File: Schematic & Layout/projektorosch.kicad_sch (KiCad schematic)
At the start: 39 parts, among them J1 Power barrel plug, J2 RJ12, U1 ATmega328-P, U2 MAX232, Y1 Crystal

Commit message: design pcb - first try
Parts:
- removed C1: 100nF, Capacitor_SMD:C_0805_2012Metric_Pad1.18x1.45mm_HandSolder, symbol Device:C
- removed R12: R, Resistor_SMD:R_0805_2012Metric_Pad1.20x1.40mm_HandSolder, symbol Device:R
- removed RESET1: SW_SPST, Button_Switch_SMD:SW_Push_1P1T_NO_6x6mm_H9.5mm, symbol Switch:SW_SPST
- D2: footprint Diode_SMD:D_0805_2012Metric_Pad1.15x1.40mm_HandSolder -> Diode_THT:D_DO-15_P2.54mm_Vertical_KathodeUp
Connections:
- net BTN1: now also U1.12 (PD6); no longer U1.23 (PC0)
- net BTN3: now also U1.6 (PD4); no longer U1.25 (PC2)
- net CTS: now also J2.5; no longer J2.6
- net GND: now also J2.1; no longer J2.3
- net RTS: now also J2.6; no longer J2.5
- net RX: now also J2.3; no longer J2.1
- net TX: no longer U1.2 (PD0), U2.12 (R1OUT)
- net at U1.28 (PC5): now also D2.2 (A)
- new net: U1.2 (PD0), U2.12 (R1OUT)
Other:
- moved on the sheet: C9

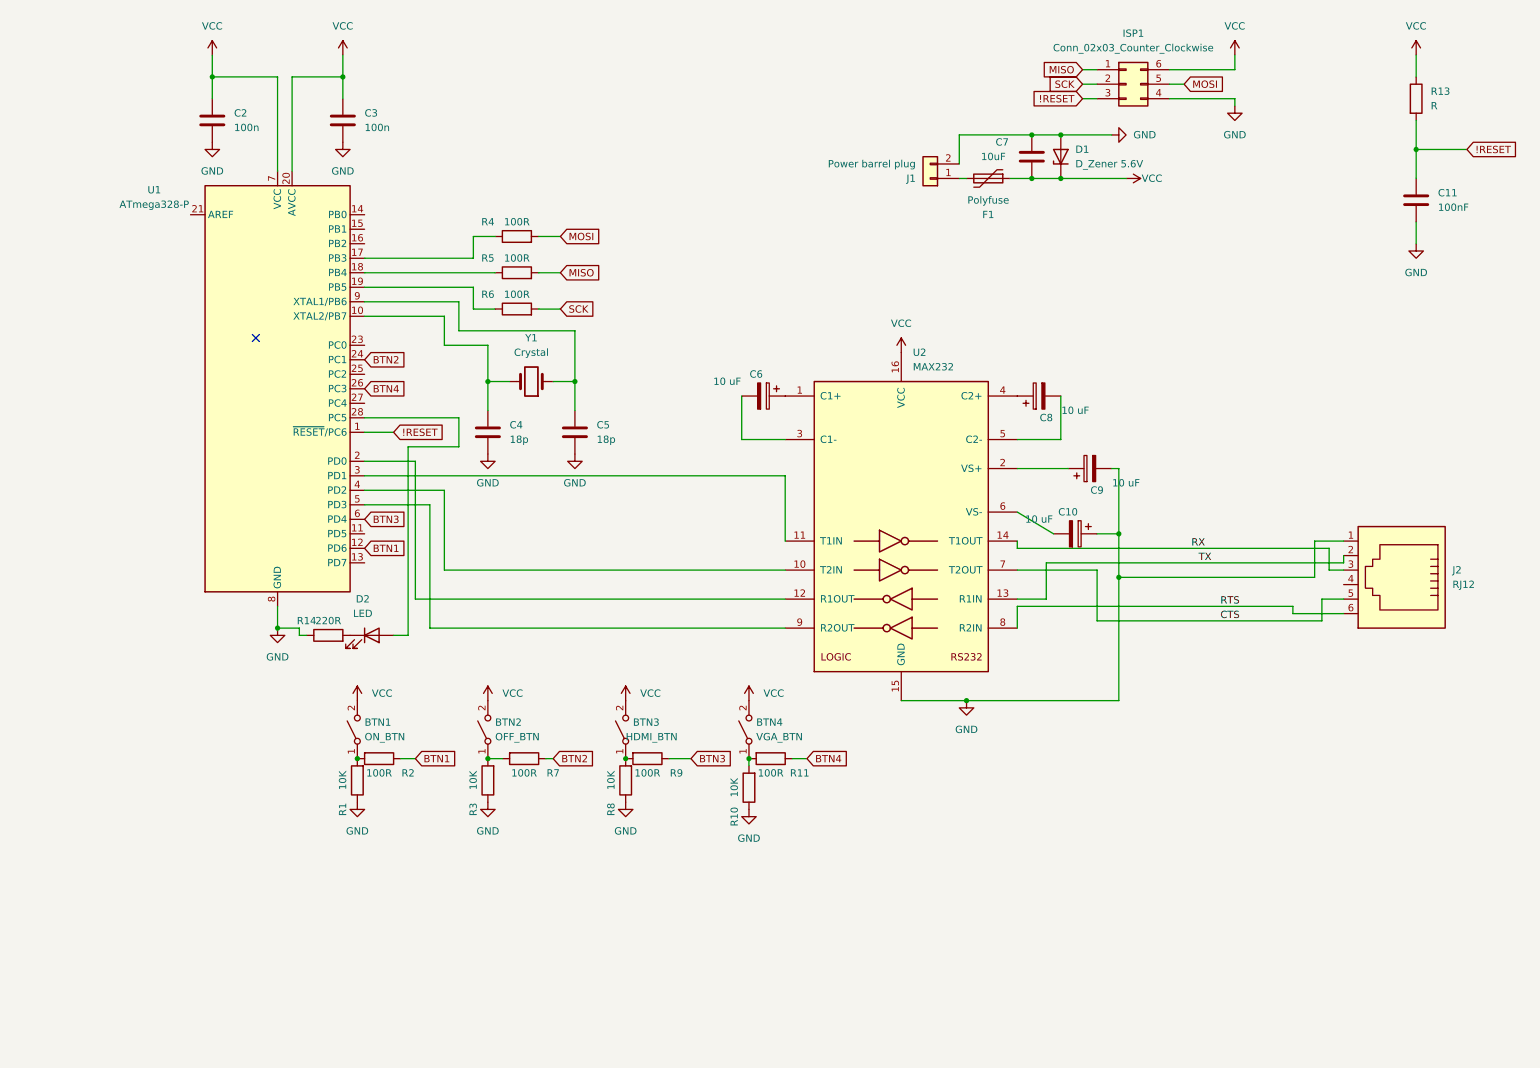
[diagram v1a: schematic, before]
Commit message: redesign layout for attiny3216
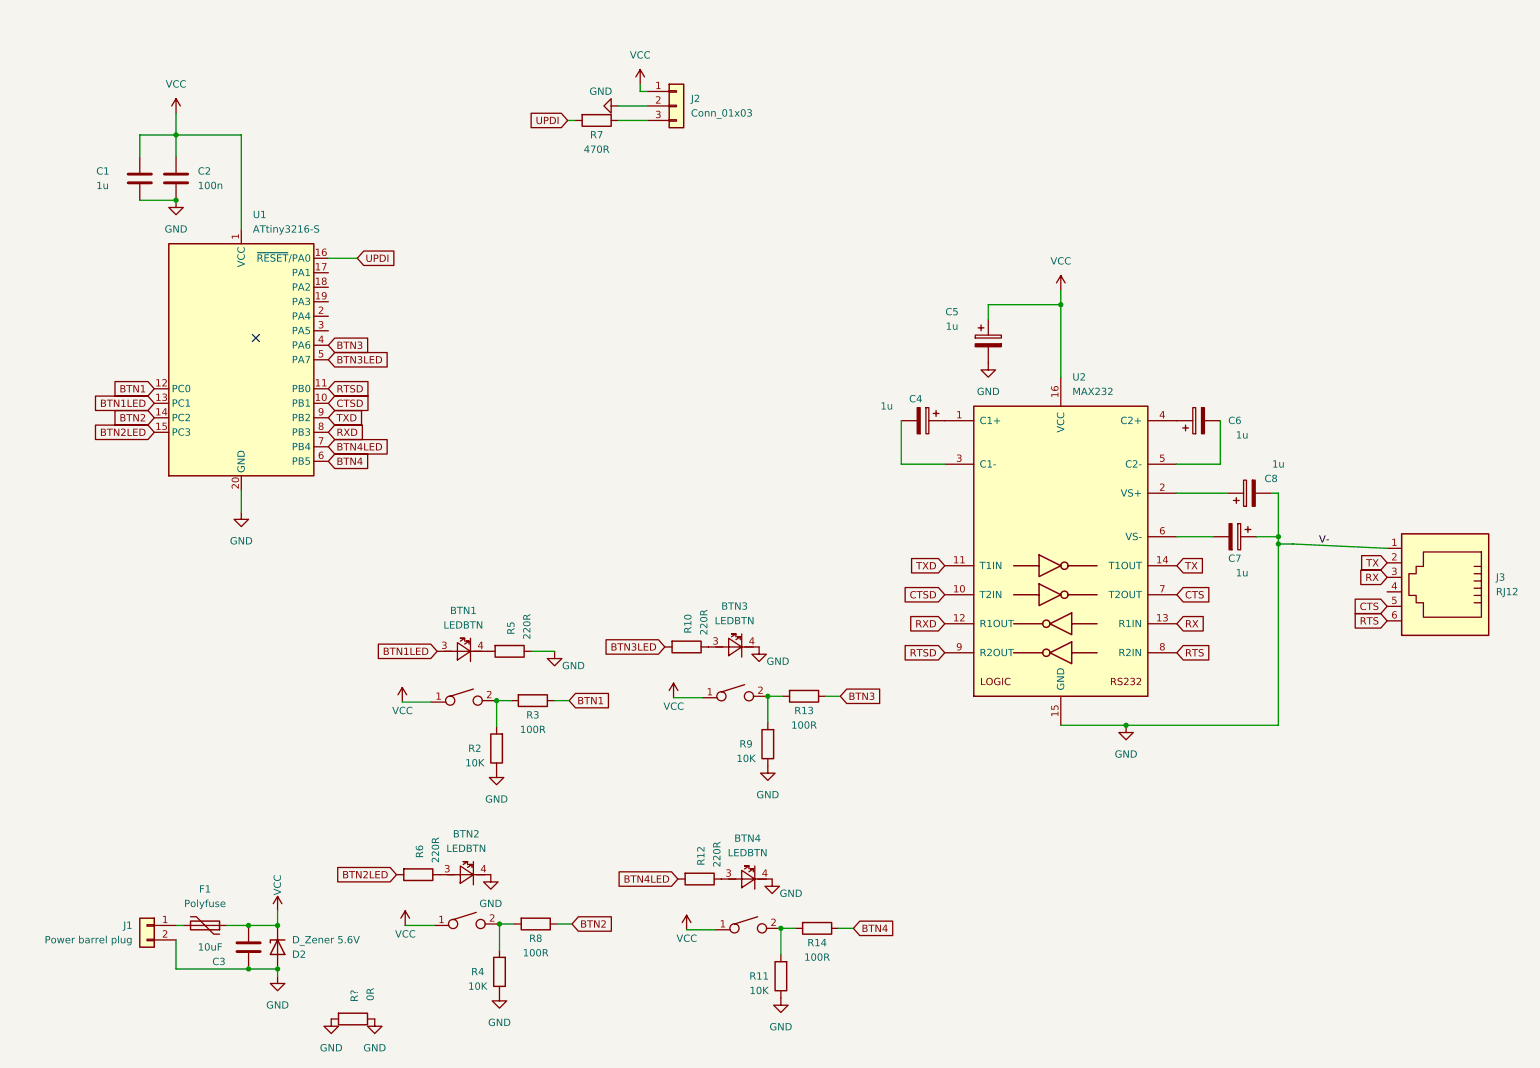
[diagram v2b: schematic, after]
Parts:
- removed BTN1: ON_BTN, Button_Switch_SMD:SW_Push_1P1T_NO_6x6mm_H9.5mm, symbol Switch:SW_SPST
- removed BTN2: OFF_BTN, Button_Switch_SMD:SW_Push_1P1T_NO_6x6mm_H9.5mm, symbol Switch:SW_SPST
- removed BTN3: HDMI_BTN, Button_Switch_SMD:SW_Push_1P1T_NO_6x6mm_H9.5mm, symbol Switch:SW_SPST
- removed BTN4: VGA_BTN, Button_Switch_SMD:SW_Push_1P1T_NO_6x6mm_H9.5mm, symbol Switch:SW_SPST
- removed C11: 100nF, Capacitor_SMD:C_0805_2012Metric_Pad1.18x1.45mm_HandSolder, symbol Device:C
- removed C3: 100n, Capacitor_SMD:C_0805_2012Metric_Pad1.18x1.45mm_HandSolder, symbol Device:C
- removed C4, C5: 18p, Capacitor_SMD:C_0603_1608Metric_Pad1.08x0.95mm_HandSolder, symbol Device:C
- removed D2: LED, Diode_THT:D_DO-15_P2.54mm_Vertical_KathodeUp, symbol Device:LED
- removed ISP1: Conn_02x03_Counter_Clockwise, Connector_PinHeader_2.00mm:PinHeader_2x03_P2.00mm_Vertical_SMD, symbol Connector_Generic:Conn_02x03_Counter_Clockwise
- removed J2: RJ12, Connector_RJ:RJ12_Amphenol_54601, symbol Connector:RJ12
- removed R3: 10K, Resistor_SMD:R_0805_2012Metric_Pad1.20x1.40mm_HandSolder, symbol Device:R
- removed U1: ATmega328-P, Package_DFN_QFN:QFN-32-1EP_5x5mm_P0.5mm_EP3.6x3.6mm_ThermalVias, symbol MCU_Microchip_ATmega:ATmega328-P
- removed Y1: Crystal, Crystal:Crystal_SMD_3225-4Pin_3.2x2.5mm_HandSoldering, symbol Device:Crystal
- added BTN1, BTN2, BTN3, BTN4: LEDBTN, ledbtn_footprint:LBTN, symbol projektorosch:LEDBTN
- added C1: 1u, Capacitor_Tantalum_SMD:CP_EIA-3216-10_Kemet-I_Pad1.58x1.35mm_HandSolder, symbol Device:C
- added C5: 1u, Capacitor_Tantalum_SMD:CP_EIA-3216-10_Kemet-I_Pad1.58x1.35mm_HandSolder, symbol Device:C_Polarized
- added J2: Conn_01x03, Connector_PinHeader_2.54mm:PinHeader_1x03_P2.54mm_Vertical, symbol Connector_Generic:Conn_01x03
- added J3: RJ12, Connector_RJ:RJ12_Amphenol_54601, symbol Connector:RJ12
- added R12: 220R, Resistor_SMD:R_0805_2012Metric_Pad1.20x1.40mm_HandSolder, symbol Device:R
- added R?: 0R, Resistor_SMD:R_0805_2012Metric_Pad1.20x1.40mm_HandSolder, symbol Device:R
- added U1: ATtiny3216-S, Package_SO:SOIC-20W_7.5x12.8mm_P1.27mm, symbol MCU_Microchip_ATtiny:ATtiny3216-S
- C3: renamed from C7; footprint Capacitor_SMD:CP_Elec_5x5.7 -> Capacitor_Tantalum_SMD:CP_EIA-3216-12_Kemet-S_Pad1.58x1.35mm_HandSolder
- C4: renamed from C6; value 10 uF -> 1u; footprint Capacitor_SMD:CP_Elec_5x5.7 -> Capacitor_Tantalum_SMD:CP_EIA-3216-10_Kemet-I_Pad1.58x1.35mm_HandSolder
- C6: renamed from C8; value 10 uF -> 1u; footprint Capacitor_SMD:CP_Elec_5x5.7 -> Capacitor_Tantalum_SMD:CP_EIA-3216-10_Kemet-I_Pad1.58x1.35mm_HandSolder
- C7: renamed from C10; value 10 uF -> 1u; footprint Capacitor_SMD:CP_Elec_5x5.7 -> Capacitor_Tantalum_SMD:CP_EIA-3216-10_Kemet-I_Pad1.58x1.35mm_HandSolder
- C8: renamed from C9; value 10 uF -> 1u; footprint Capacitor_SMD:CP_Elec_5x5.7 -> Capacitor_Tantalum_SMD:CP_EIA-3216-10_Kemet-I_Pad1.58x1.35mm_HandSolder
- F1: footprint Fuse:Fuse_BelFuse_0ZRE0005FF_L8.3mm_W3.8mm -> Fuse:Fuse_1812_4532Metric_Pad1.30x3.40mm_HandSolder
- R10: value 10K -> 220R
- R11, R4, R9: value 100R -> 10K
- R13: value R -> 100R
- R14: value 220R -> 100R
- R5, R6: value 100R -> 220R
- R7: value 100R -> 470R
- R8: value 10K -> 100R
- U2: footprint Package_SO:HTSSOP-16-1EP_4.4x5mm_P0.65mm_EP3.4x5mm_Mask2.46x2.31mm -> Package_DIP:DIP-16_W7.62mm
- renumbered D1 to D2, R1 to R2, R2 to R3
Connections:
- net !RESET is gone; now on an unnamed net: R13.2
- net BTN1: now also U1.12 (PC0)
- net BTN2: now also R8.1, U1.14 (PC2); no longer R7.1
- net BTN3: now also R13.1, U1.4 (PA6); no longer R9.1
- net BTN4: now also R14.1, U1.6 (PB5); no longer R11.1
- net CTS: now also J3.5
- net GND: now also R11.1, R4.1, R5.1, R9.1, BTN2.4, BTN3.4, BTN4.4, C1.2, C5.2, J2.2 (Pin_2), J3.1, R?.1, R?.2, U1.20 (GND); no longer R10.1, R14.1, R8.1
- net RTS: now also J3.6
- net RX: now also U2.13 (R1IN), J3.3; no longer U2.14 (T1OUT)
- net TX: now also U2.14 (T1OUT), J3.2; no longer U2.13 (R1IN)
- net VCC: now also BTN1.1, BTN2.1, BTN3.1, BTN4.1, C1.1, C5.1, J2.1 (Pin_1), U1.1 (VCC); no longer R13.1
- net at R6.1: now also BTN2.3
- net UPDI: now reaches R7.2
- net UPDI: now also U1.16 (~{RESET}/PA0)
- net at R11.2: now also R14.2, BTN4.2; no longer R10.2
- net at R2.2, R3.2: now also BTN1.2
- net CTSD: now reaches U2.10 (T2IN)
- net CTSD: now also U1.10 (PB1)
- net TXD: now reaches U2.11 (T1IN)
- net TXD: now also U1.9 (PB2)
- net RXD: now reaches U2.12 (R1OUT)
- net RXD: now also U1.8 (PB3)
- net RTSD: now reaches U2.9 (R2OUT)
- net RTSD: now also U1.11 (PB0)
- net at R9.2: now also BTN3.2; no longer R8.2
- net MISO: no longer names the net of R5.2
- net MISO: now also BTN1.4
- net MOSI: no longer names the net of R4.2
- net MOSI: now also R8.2, BTN2.2
- net SCK renamed BTN2LED
- net BTN2LED: now also U1.15 (PC3)
- new net: BTN4.3, R12.1
- new net: J2.3 (Pin_3), R7.1
- new net: BTN3.3, R10.1
- new net BTN1LED: BTN1.3, U1.13 (PC1)
- new net BTN3LED: R10.2, U1.5 (PA7)
- new net BTN4LED: R12.2, U1.7 (PB4)
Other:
- moved on the sheet: C2, C3, C4, C6, C7, C8, D2, F1, J1, R2, R3, U2

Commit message: attinty3216-remeljuk-final
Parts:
- removed J1: Power barrel plug, Connector_BarrelJack:BarrelJack_CLIFF_FC681465S_SMT_Horizontal, symbol Connector_Generic:Conn_01x02
- removed R11, R2, R4, R9: 10K, Resistor_SMD:R_0805_2012Metric_Pad1.20x1.40mm_HandSolder, symbol Device:R
- removed R13, R14, R3, R8: 100R, Resistor_SMD:R_0805_2012Metric_Pad1.20x1.40mm_HandSolder, symbol Device:R
- removed R?: 0R, Resistor_SMD:R_0805_2012Metric_Pad1.20x1.40mm_HandSolder, symbol Device:R
- added J1: Barrel_Jack_Switch, Connector_BarrelJack:BarrelJack_Horizontal, symbol Connector:Barrel_Jack_Switch
- renumbered D2 to D1, R12 to R10, R6 to R2, R7 to R8, R10 to R9
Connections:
- net BTN1: now also BTN1.2, U1.14 (PC2); no longer U1.12 (PC0)
- net BTN1LED: now also R5.2, U1.15 (PC3); no longer BTN1.3, U1.13 (PC1)
- net BTN2: now also BTN2.2, U1.12 (PC0); no longer U1.14 (PC2)
- net BTN2LED: now also U1.13 (PC1); no longer U1.15 (PC3)
- net BTN3: now also BTN3.2, U1.17 (PA1); no longer U1.4 (PA6)
- net BTN3LED: now also U1.18 (PA2); no longer U1.5 (PA7)
- net BTN4: now also BTN4.2, U1.2 (PA4); no longer U1.6 (PB5)
- net BTN4LED: now also U1.5 (PA7); no longer U1.7 (PB4)
- net GND: now also BTN1.1, BTN1.4, BTN2.1, BTN3.1, BTN4.1, U1.3 (PA5), U1.4 (PA6), J1.2, J1.3; no longer R5.1
- net VCC: no longer BTN1.1, BTN2.1, BTN3.1, BTN4.1
- net at F1.2: now also J1.1
- new net: BTN1.3, R5.1
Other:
- moved on the sheet: R5

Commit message: SEM ProjektoroSCH Revision 2
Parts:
- removed BTN1, BTN2, BTN3, BTN4: LEDBTN, ledbtn_footprint:LBTN, symbol projektorosch:LEDBTN
- removed C1: 1u, Capacitor_Tantalum_SMD:CP_EIA-3216-10_Kemet-I_Pad1.58x1.35mm_HandSolder, symbol Device:C
- removed C2: 100n, Capacitor_SMD:C_0805_2012Metric_Pad1.18x1.45mm_HandSolder, symbol Device:C
- removed C3: 10uF, Capacitor_Tantalum_SMD:CP_EIA-3216-12_Kemet-S_Pad1.58x1.35mm_HandSolder, symbol Device:C
- removed C5, C7, C8: 1u, Capacitor_Tantalum_SMD:CP_EIA-3216-10_Kemet-I_Pad1.58x1.35mm_HandSolder, symbol Device:C_Polarized
- removed D1: D_Zener 5.6V, Diode_SMD:Nexperia_CFP3_SOD-123W, symbol Device:D_Zener
- removed F1: Polyfuse, Fuse:Fuse_1812_4532Metric_Pad1.30x3.40mm_HandSolder, symbol Device:Polyfuse
- removed J1: Barrel_Jack_Switch, Connector_BarrelJack:BarrelJack_Horizontal, symbol Connector:Barrel_Jack_Switch
- removed J2: Conn_01x03, Connector_PinHeader_2.54mm:PinHeader_1x03_P2.54mm_Vertical, symbol Connector_Generic:Conn_01x03
- removed J3: RJ12, Connector_RJ:RJ12_Amphenol_54601, symbol Connector:RJ12
- removed R10, R2, R5, R9: 220R, Resistor_SMD:R_0805_2012Metric_Pad1.20x1.40mm_HandSolder, symbol Device:R
- removed R8: 470R, Resistor_SMD:R_0805_2012Metric_Pad1.20x1.40mm_HandSolder, symbol Device:R
- removed U1: ATtiny3216-S, Package_SO:SOIC-20W_7.5x12.8mm_P1.27mm, symbol MCU_Microchip_ATtiny:ATtiny3216-S
- removed U2: MAX232, Package_DIP:DIP-16_W7.62mm, symbol Interface_UART:MAX232
- added C1, C2, C3: 0.1uF, Capacitor_SMD:C_0805_2012Metric_Pad1.18x1.45mm_HandSolder, symbol Device:C_Polarized
- added C10, C9: 22pF, Capacitor_SMD:C_0805_2012Metric_Pad1.18x1.45mm_HandSolder, symbol Device:C_Small
- added C5, C7, C8: 0.1uF, Capacitor_SMD:C_0805_2012Metric_Pad1.18x1.45mm_HandSolder, symbol Device:C_Small
- added J1: Power, Connector_Phoenix_MC:PhoenixContact_MC_1,5_2-G-3.5_1x02_P3.50mm_Horizontal, symbol Connector:Screw_Terminal_01x02
- added J2: RS232, Connector_Phoenix_MC:PhoenixContact_MC_1,5_3-G-3.5_1x03_P3.50mm_Horizontal, symbol Connector:Screw_Terminal_01x03
- added J3: Programmer, Connector_PinHeader_2.54mm:PinHeader_1x06_P2.54mm_Vertical, symbol Connector:Conn_01x06_Pin
- added J4: ISP, Connector_PinHeader_2.54mm:PinHeader_2x03_P2.54mm_Vertical, symbol Connector_Generic:Conn_02x03_Odd_Even
- added R1, R2, R3, R4: 150, Resistor_SMD:R_0805_2012Metric_Pad1.20x1.40mm_HandSolder, symbol Device:R_Small
- added R5, R6, R7, R8, R9: 10k, Resistor_SMD:R_0805_2012Metric_Pad1.20x1.40mm_HandSolder, symbol Device:R_Small
- added SW1, SW2, SW3, SW4: SW_SPST, symbol ledbtn:Marquardt
- added SW5: Reset, Button_Switch_SMD:SW_Push_1P1T_NO_6x6mm_H9.5mm, symbol Switch:SW_SPST
- added TP1: 5V, TestPoint:TestPoint_Pad_D2.5mm, symbol Connector:TestPoint
- added TP2: GND, TestPoint:TestPoint_Pad_D2.5mm, symbol Connector:TestPoint
- added TP3: 232-RX, TestPoint:TestPoint_Pad_D2.5mm, symbol Connector:TestPoint
- added TP4: 232-TX, TestPoint:TestPoint_Pad_D2.5mm, symbol Connector:TestPoint
- added U1: MAX232, Package_SO:SOP-16_3.9x9.9mm_P1.27mm, symbol Interface_UART:MAX232
- added U2: ATmega328P-A, Package_QFP:TQFP-32_7x7mm_P0.8mm, symbol MCU_Microchip_ATmega:ATmega328P-A
- added Y1: 16MHz, Crystal:Crystal_SMD_HC49-SD_HandSoldering, symbol Device:Crystal
- C4, C6: value 1u -> 0.1uF; footprint Capacitor_Tantalum_SMD:CP_EIA-3216-10_Kemet-I_Pad1.58x1.35mm_HandSolder -> Capacitor_SMD:C_0805_2012Metric_Pad1.18x1.45mm_HandSolder
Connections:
- net GND: now also C4.1, C10.1, C2.2, C5.1, C7.1, C9.1, J1.1 (Pin_1), J2.1 (Pin_1), J3.1 (Pin_1), J3.2 (Pin_2), J4.6 (Pin_6), SW1.1 (A), SW1.4 (K), SW2.1 (A), SW2.4 (K), SW3.1 (A), SW3.4 (K), SW4.1 (A), SW4.4 (K), SW5.1 (A), TP2.1, U1.15 (GND), U2.21 (GND), U2.3 (GND), U2.5 (GND)
- net at C6.1: now also U1.2 (VS+)
- net +5V: now reaches C6.2
- net +5V: now also C2.1, C7.2, J1.2 (Pin_2), J3.3 (Pin_3), J4.2 (Pin_2), R5.2, R6.2, R7.2, R8.2, R9.2, TP1.1, U1.16 (VCC), U2.18 (AVCC), U2.4 (VCC), U2.6 (VCC)
- net at C4.2: now also U1.6 (VS-)
- new net: R1.1, SW1.3 (A)
- new net: R2.1, SW2.3 (A)
- new net: C10.2, U2.8 (XTAL2/PB7), Y1.1
- new net: C1.1, U1.1 (C1+)
- new net: C1.2, U1.3 (C1-)
- new net: C3.1, U1.4 (C2+)
- new net: C3.2, U1.5 (C2-)
- new net: R4.1, SW4.3 (A)
- new net: C5.2, U2.20 (AREF)
- new net: C9.2, U2.7 (XTAL1/PB6), Y1.2
- new net: R3.1, SW3.3 (A)
- new net 232-RX: J2.3 (Pin_3), TP3.1, U1.8 (R2IN)
- new net 232-TX: J2.2 (Pin_2), TP4.1, U1.14 (T1OUT)
- new net BTN-1: R5.1, SW1.2 (B), U2.26 (PC3)
- new net BTN-2: R6.1, SW2.2 (B), U2.27 (PC4)
- new net BTN-3: R7.1, SW3.2 (B), U2.25 (PC2)
- new net BTN-4: R8.1, SW4.2 (B), U2.28 (PC5)
- new net MCU-RX: J3.5 (Pin_5), U1.9 (R2OUT), U2.30 (PD0)
- new net MCU-TX: J3.4 (Pin_4), U1.11 (T1IN), U2.31 (PD1)
- new net MISO: J4.1 (Pin_1), U2.16 (PB4)
- new net MOSI: J4.4 (Pin_4), U2.15 (PB3)
- new net PROG-DTR: C8.2, J3.6 (Pin_6)
- new net PWM-1: R1.2, U2.13 (PB1)
- new net PWM-2: R2.2, U2.10 (PD6)
- new net PWM-3: R3.2, U2.14 (PB2)
- new net PWM-4: R4.2, U2.9 (PD5)
- new net RST: C8.1, J4.5 (Pin_5), R9.1, SW5.2 (B), U2.29 (~{RESET}/PC6)
- new net SCK: J4.3 (Pin_3), U2.17 (PB5)
- no-connect marks 1 -> 13
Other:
- note added: "GND CTS VCC RX TX DTR"
- company: SEM -> Schönherz Elektronikai Műhely
- title: ProjektoroSCH -> TávirányítóSCH
